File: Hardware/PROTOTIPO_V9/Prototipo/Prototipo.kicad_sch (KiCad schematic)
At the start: 1 part, among them U1 YAAJ_BluePill_Part_Like_SWD_B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

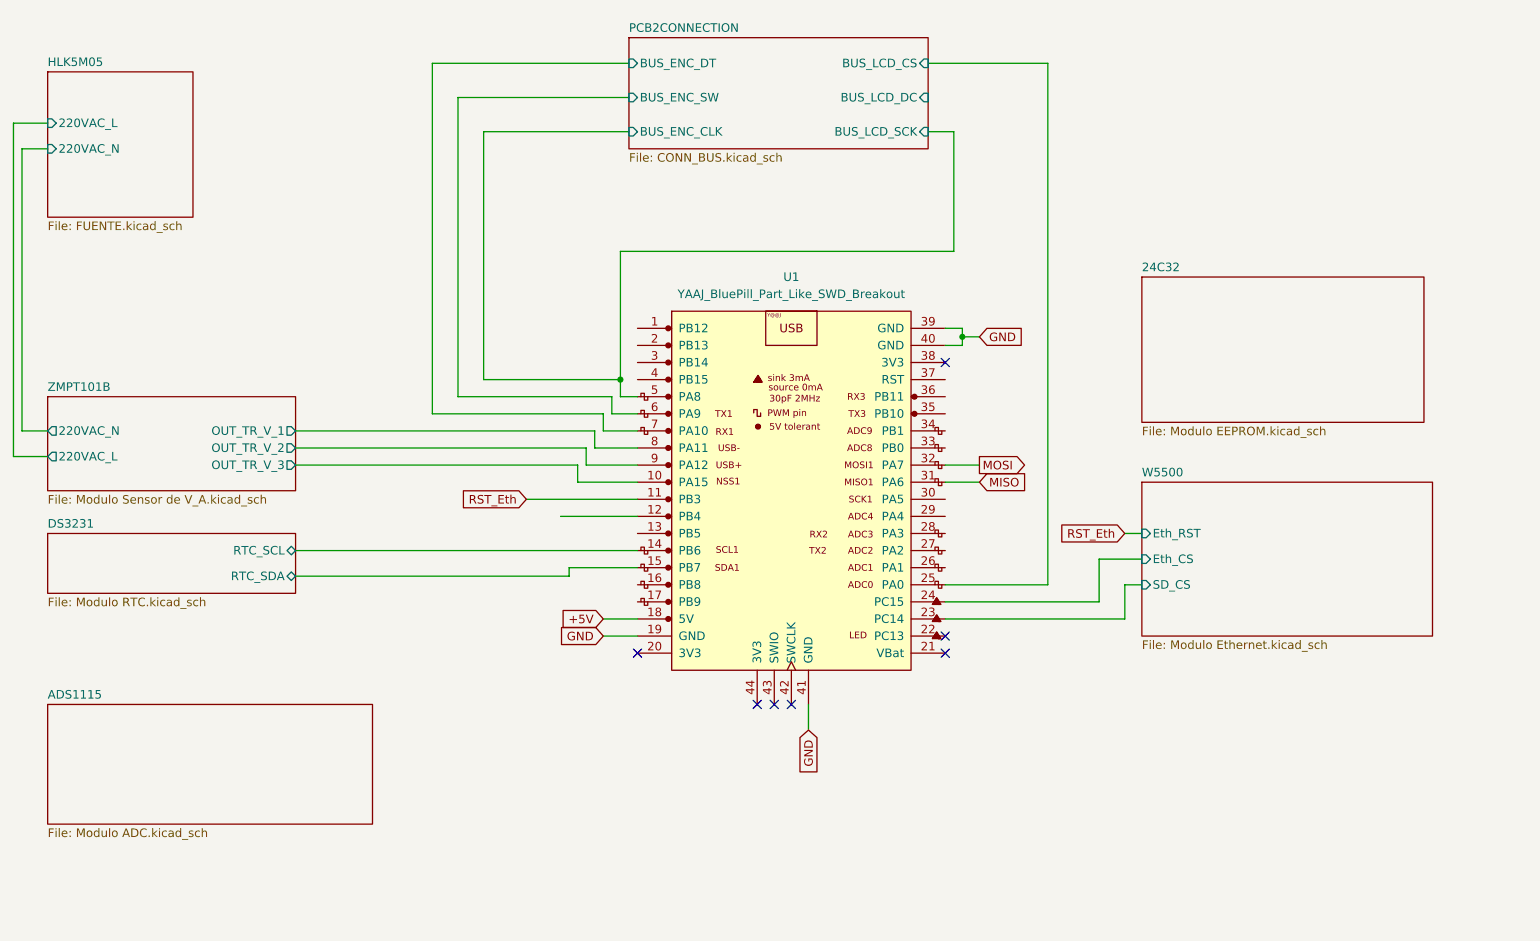
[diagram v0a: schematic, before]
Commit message: sch ILI9341 y sch ADS1115
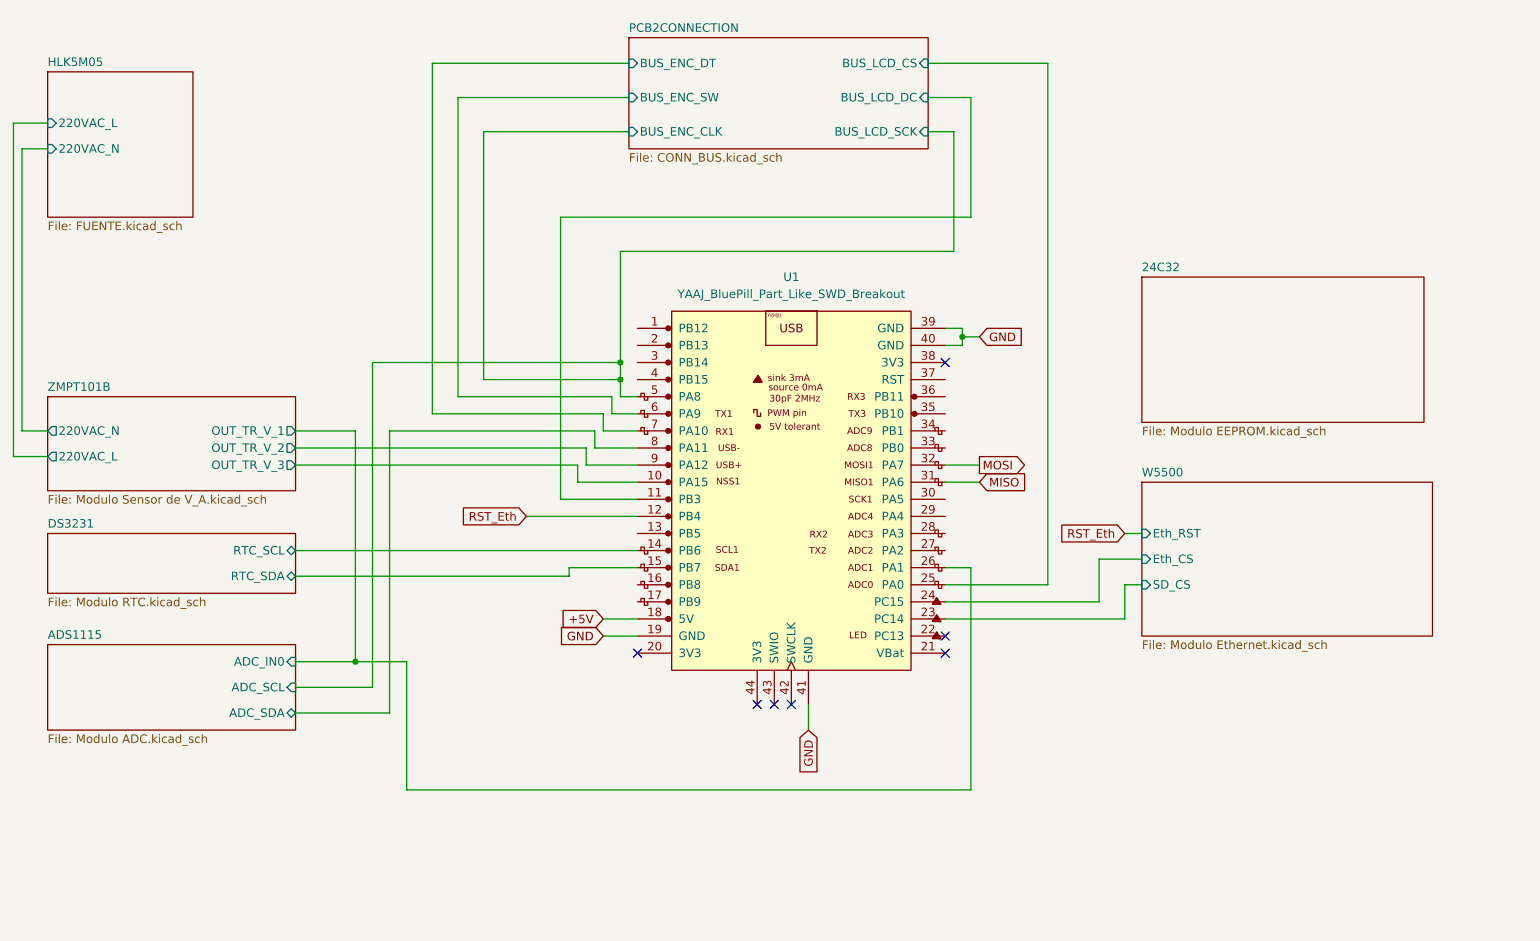
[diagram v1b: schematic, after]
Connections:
- net PCB2CONNECTION/BUS_LCD_DC: now also U1.11 (PB3)
- net RST_Eth: now also U1.12 (PB4); no longer U1.11 (PB3)
- net ADS1115/ADC_IN0: now reaches U1.26 (PA1)
- net PCB2CONNECTION/BUS_ENC_CLK renamed ADS1115/ADC_SCL
- net ZMPT101B/OUT_TR_V_1 renamed ADS1115/ADC_SDA
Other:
- sheet ADS1115 ports: added ADC_IN0, ADC_SCL, ADC_SDA; removed none
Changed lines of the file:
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@@
 	(paper "A4")
+	(junction
+		(at 82.55 125.73)
+		(diameter 0)
+		(color 0 0 0 0)
+	)
 	(junction
 		(at 172.72 77.47)
@@
 	)
 	(junction
+		(at 121.92 81.28)
+		(diameter 0)
+		(color 0 0 0 0)
+	)
+	(junction
 		(at 121.92 83.82)
 		(diameter 0)
@@
 	(wire
 		(pts
+			(xy 173.99 41.91) (xy 173.99 59.69)
+		)
+		(stroke
+			(width 0)
+			(type default)
+		)
+	)
+	(wire
+		(pts
 			(xy 36.83 91.44) (xy 33.02 91.44)
 		)
@@
 	(wire
 		(pts
+			(xy 85.09 81.28) (xy 85.09 129.54)
+		)
+		(stroke
+			(width 0)
+			(type default)
+		)
+	)
+	(wire
+		(pts
 			(xy 97.79 41.91) (xy 123.19 41.91)
 		)
@@
 	(wire
 		(pts
+			(xy 121.92 81.28) (xy 121.92 83.82)
+		)
+		(stroke
+			(width 0)
+			(type default)
+		)
+	)
+	(wire
+		(pts
+			(xy 85.09 129.54) (xy 73.66 129.54)
+		)
+		(stroke
+			(width 0)
+			(type default)
+		)
+	)
+	(wire
+		(pts
 			(xy 171.45 46.99) (xy 171.45 64.77)
 		)
@@
 	(wire
 		(pts
+			(xy 85.09 81.28) (xy 121.92 81.28)
+		)
+		(stroke
+			(width 0)
+			(type default)
+		)
+	)
+	(wire
+		(pts
 			(xy 73.66 113.03) (xy 114.3 113.03)
 		)
@@
 	(wire
 		(pts
+			(xy 87.63 91.44) (xy 87.63 133.35)
+		)
+		(stroke
+			(width 0)
+			(type default)
+		)
+	)
+	(wire
+		(pts
+			(xy 87.63 133.35) (xy 73.66 133.35)
+		)
+		(stroke
+			(width 0)
+			(type default)
+		)
+	)
+	(wire
+		(pts
 			(xy 114.3 111.76) (xy 124.46 111.76)
 		)
@@
 	(wire
 		(pts
+			(xy 113.03 59.69) (xy 113.03 101.6)
+		)
+		(stroke
+			(width 0)
+			(type default)
+		)
+	)
+	(wire
+		(pts
 			(xy 121.92 86.36) (xy 124.46 86.36)
 		)
@@
 	(wire
 		(pts
+			(xy 82.55 125.73) (xy 82.55 91.44)
+		)
+		(stroke
+			(width 0)
+			(type default)
+		)
+	)
+	(wire
+		(pts
+			(xy 113.03 101.6) (xy 124.46 101.6)
+		)
+		(stroke
+			(width 0)
+			(type default)
+		)
+	)
+	(wire
+		(pts
 			(xy 149.86 135.89) (xy 149.86 132.08)
 		)
@@
 	(wire
 		(pts
+			(xy 173.99 144.78) (xy 173.99 111.76)
+		)
+		(stroke
+			(width 0)
+			(type default)
+		)
+	)
+	(wire
+		(pts
 			(xy 172.72 77.47) (xy 175.26 77.47)
 		)
@@
 	(wire
 		(pts
+			(xy 90.17 125.73) (xy 90.17 144.78)
+		)
+		(stroke
+			(width 0)
+			(type default)
+		)
+	)
+	(wire
+		(pts
 			(xy 170.18 119.38) (xy 196.85 119.38)
 		)
@@
 	(wire
 		(pts
-			(xy 107.95 101.6) (xy 124.46 101.6)
+			(xy 107.95 104.14) (xy 124.46 104.14)
+		)
+		(stroke
+			(width 0)
+			(type default)
+		)
+	)
+	(wire
+		(pts
+			(xy 90.17 144.78) (xy 173.99 144.78)
 		)
 		(stroke
@@
 	(wire
 		(pts
+			(xy 173.99 59.69) (xy 113.03 59.69)
+		)
+		(stroke
+			(width 0)
+			(type default)
+		)
+	)
+	(wire
+		(pts
 			(xy 118.11 93.98) (xy 124.46 93.98)
 		)
@@
 	(wire
 		(pts
+			(xy 82.55 125.73) (xy 90.17 125.73)
+		)
+		(stroke
+			(width 0)
+			(type default)
+		)
+	)
+	(wire
+		(pts
+			(xy 173.99 111.76) (xy 170.18 111.76)
+		)
+		(stroke
+			(width 0)
+			(type default)
+		)
+	)
+	(wire
+		(pts
 			(xy 116.84 96.52) (xy 124.46 96.52)
 		)
@@
 	(wire
 		(pts
-			(xy 113.03 104.14) (xy 124.46 104.14)
-		)
-		(stroke
-			(width 0)
-			(type default)
-		)
-	)
-	(wire
-		(pts
 			(xy 33.02 49.53) (xy 36.83 49.53)
 		)
@@
 	(wire
 		(pts
-			(xy 73.66 91.44) (xy 118.11 91.44)
+			(xy 167.64 41.91) (xy 173.99 41.91)
+		)
+		(stroke
+			(width 0)
+			(type default)
+		)
+	)
+	(wire
+		(pts
+			(xy 73.66 91.44) (xy 82.55 91.44)
 		)
 		(stroke
@@
 	(wire
 		(pts
+			(xy 118.11 91.44) (xy 87.63 91.44)
+		)
+		(stroke
+			(width 0)
+			(type default)
+		)
+	)
+	(wire
+		(pts
 			(xy 172.72 77.47) (xy 172.72 78.74)
 		)
@@
 	(wire
 		(pts
-			(xy 121.92 64.77) (xy 121.92 83.82)
+			(xy 73.66 125.73) (xy 82.55 125.73)
+		)
+		(stroke
+			(width 0)
+			(type default)
+		)
+	)
+	(wire
+		(pts
+			(xy 121.92 64.77) (xy 121.92 81.28)
 		)
 		(stroke
@@
 	(global_label "RST_Eth"
 		(shape input)
-		(at 107.95 101.6 180)
+		(at 107.95 104.14 180)
 		(fields_autoplaced yes)
 		(effects
@@
 		)
 		(property "Intersheetrefs" "${INTERSHEET_REFS}"
-			(at 97.5264 101.6 0)
+			(at 97.5264 104.14 0)
 			(effects
 				(font
@@
 	)
 	(sheet
-		(at 36.83 132.08)
-		(size 48.26 17.78)
+		(at 36.83 123.19)
+		(size 36.83 12.7)
 		(exclude_from_sim no)
 		(in_bom yes)
@@
 		)
 		(property "Sheetname" "ADS1115"
-			(at 36.83 131.3684 0)
+			(at 36.83 122.4784 0)
 			(effects
 				(font
@@
 		)
 		(property "Sheetfile" "Modulo ADC.kicad_sch"
-			(at 36.83 150.4446 0)
+			(at 36.83 136.4746 0)
 			(effects
 				(font
@@
 			)
 		)
+		(pin "ADC_SCL" input
+			(at 73.66 129.54 0)
+			(effects
+				(font
+					(size 1.27 1.27)
+				)
+				(justify right)
+			)
+		)
+		(pin "ADC_SDA" bidirectional
+			(at 73.66 133.35 0)
+			(effects
+				(font
+					(size 1.27 1.27)
+				)
+				(justify right)
+			)
+		)
+		(pin "ADC_IN0" input
+			(at 73.66 125.73 0)
+			(effects
+				(font
+					(size 1.27 1.27)
+				)
+				(justify right)
+			)
+		)

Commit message: sch ILI9341
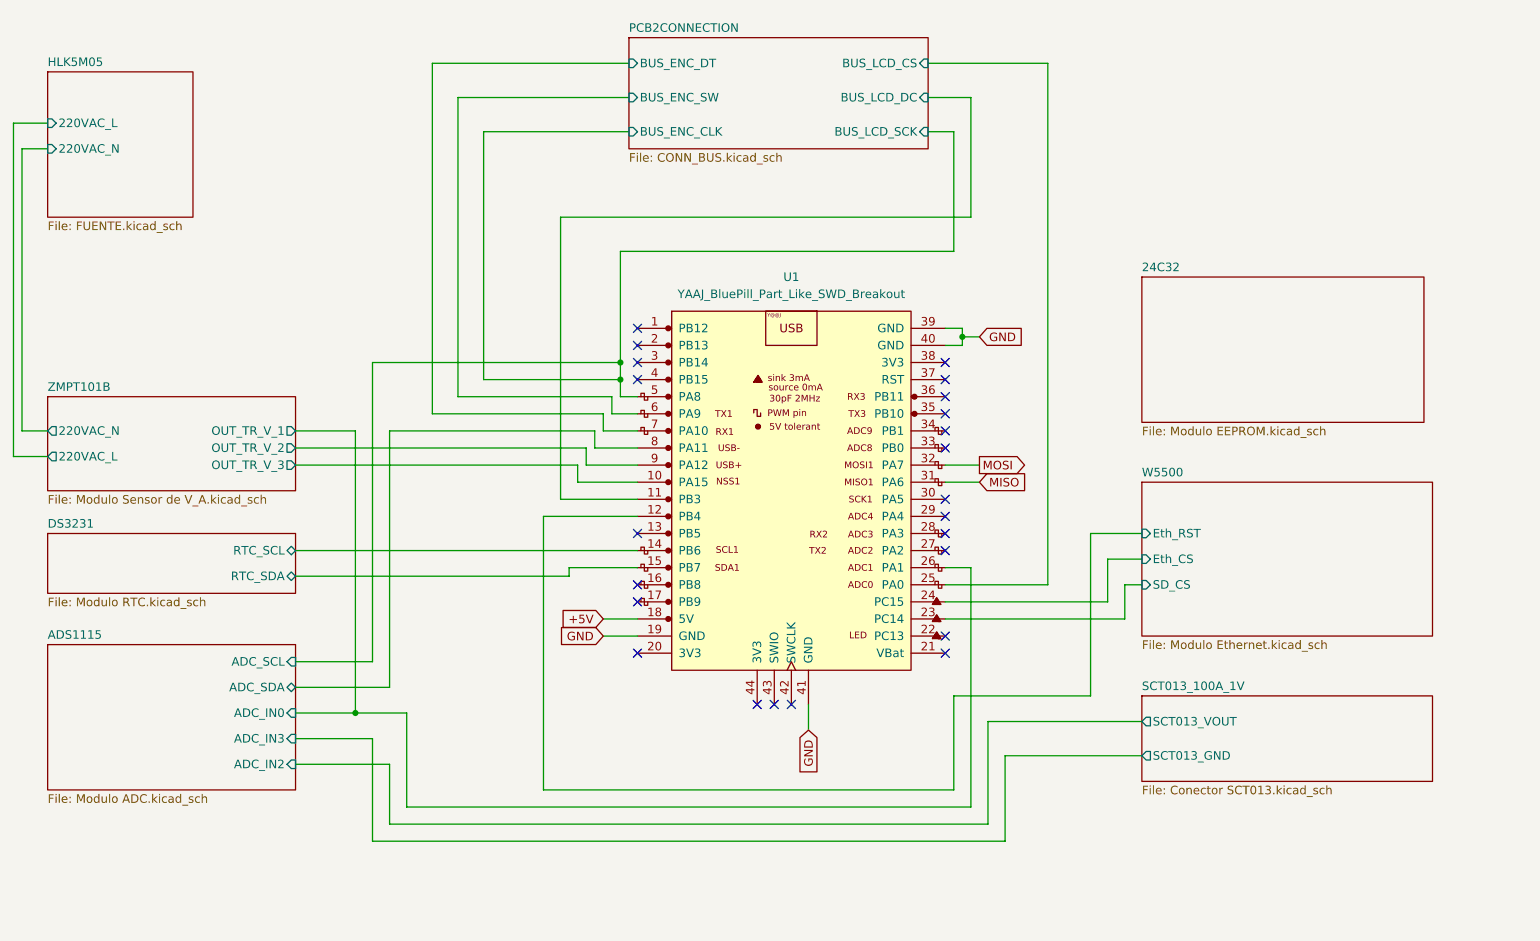
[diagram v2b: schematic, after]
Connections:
- net RST_Eth renamed W5500/Eth_RST
- no-connect marks 7 -> 23
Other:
- added sheet SCT013_100A_1V (Conector SCT013.kicad_sch)
- sheet ADS1115 ports: added ADC_IN2, ADC_IN3; removed none

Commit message: ERC: 0 errores
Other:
- sheet PCB2CONNECTION ports: added none; removed BUS_LCD_SCK
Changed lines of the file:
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@@
-	)
-	(junction
-		(at 121.92 81.28)
-		(diameter 0)
-		(color 0 0 0 0)
 	)
 	(junction
@@
 	(wire
 		(pts
-			(xy 171.45 46.99) (xy 171.45 64.77)
-		)
-		(stroke
-			(width 0)
-			(type default)
-		)
-	)
-	(wire
-		(pts
 			(xy 194.31 110.49) (xy 199.39 110.49)
 		)
@@
 	(wire
 		(pts
-			(xy 167.64 46.99) (xy 171.45 46.99)
-		)
-		(stroke
-			(width 0)
-			(type default)
-		)
-	)
-	(wire
-		(pts
 			(xy 115.57 96.52) (xy 115.57 99.06)
 		)
@@
 	(wire
 		(pts
-			(xy 171.45 64.77) (xy 121.92 64.77)
-		)
-		(stroke
-			(width 0)
-			(type default)
-		)
-	)
-	(wire
-		(pts
 			(xy 87.63 140.97) (xy 87.63 149.86)
 		)
@@
 		(pts
 			(xy 170.18 96.52) (xy 175.26 96.52)
-		)
-		(stroke
-			(width 0)
-			(type default)
-		)
-	)
-	(wire
-		(pts
-			(xy 121.92 64.77) (xy 121.92 81.28)
 		)
 		(stroke
@@
 			(effects
 				(font
-					(size 1.27 1.27)
-				)
-				(justify right)
-			)
-		)
-		(pin "BUS_LCD_SCK" input
-			(at 167.64 46.99 0)
-			(effects
-				(font

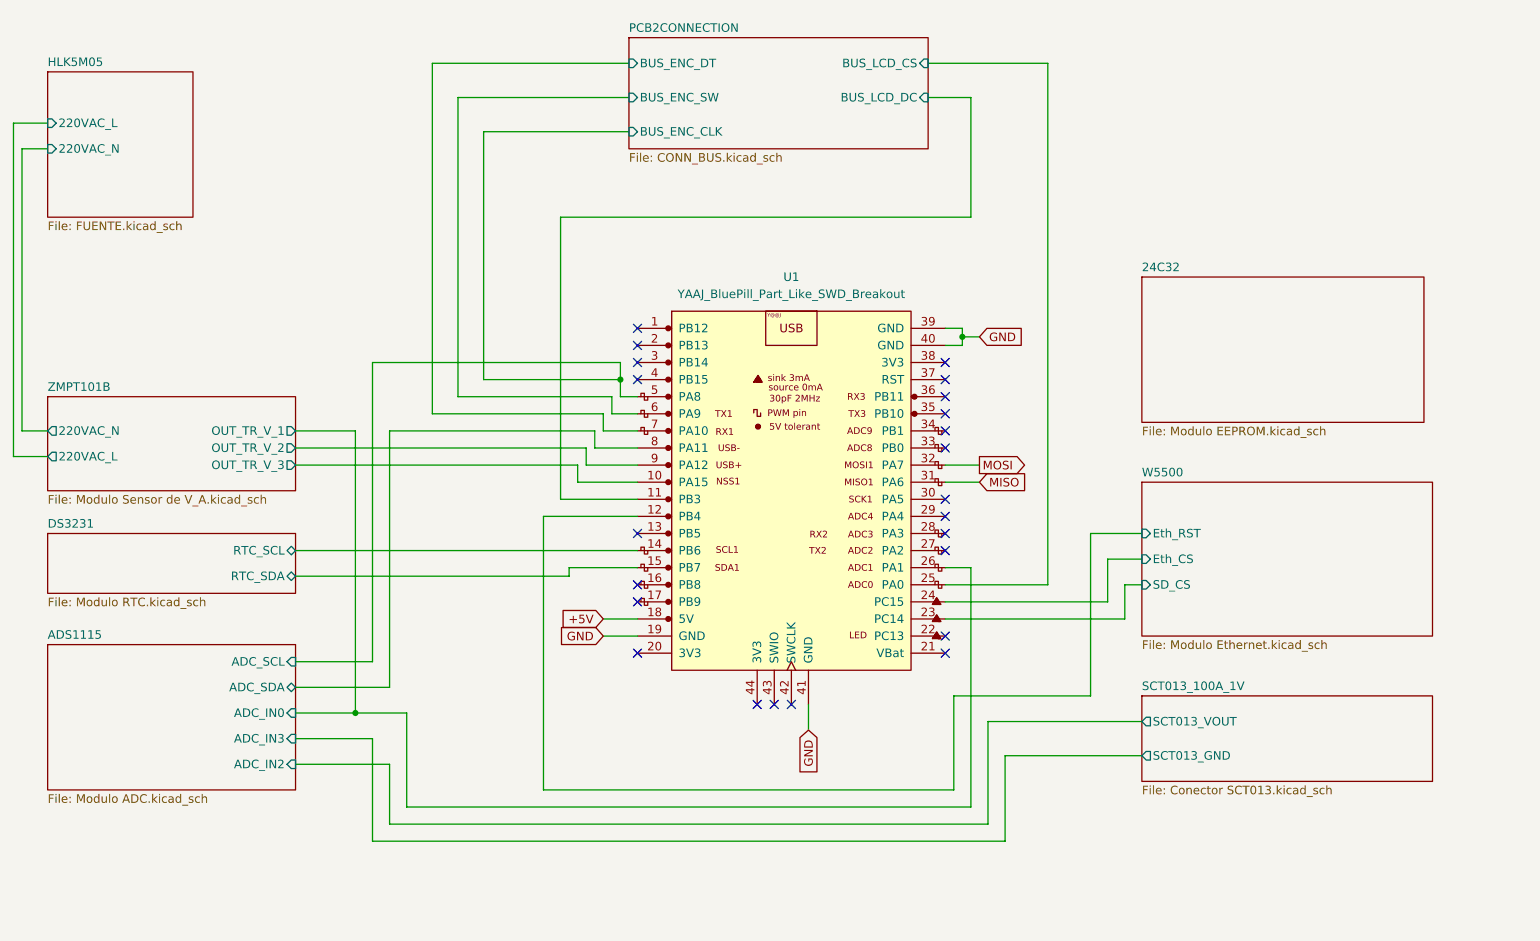
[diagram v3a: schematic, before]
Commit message: Esquematico TR de Corriente
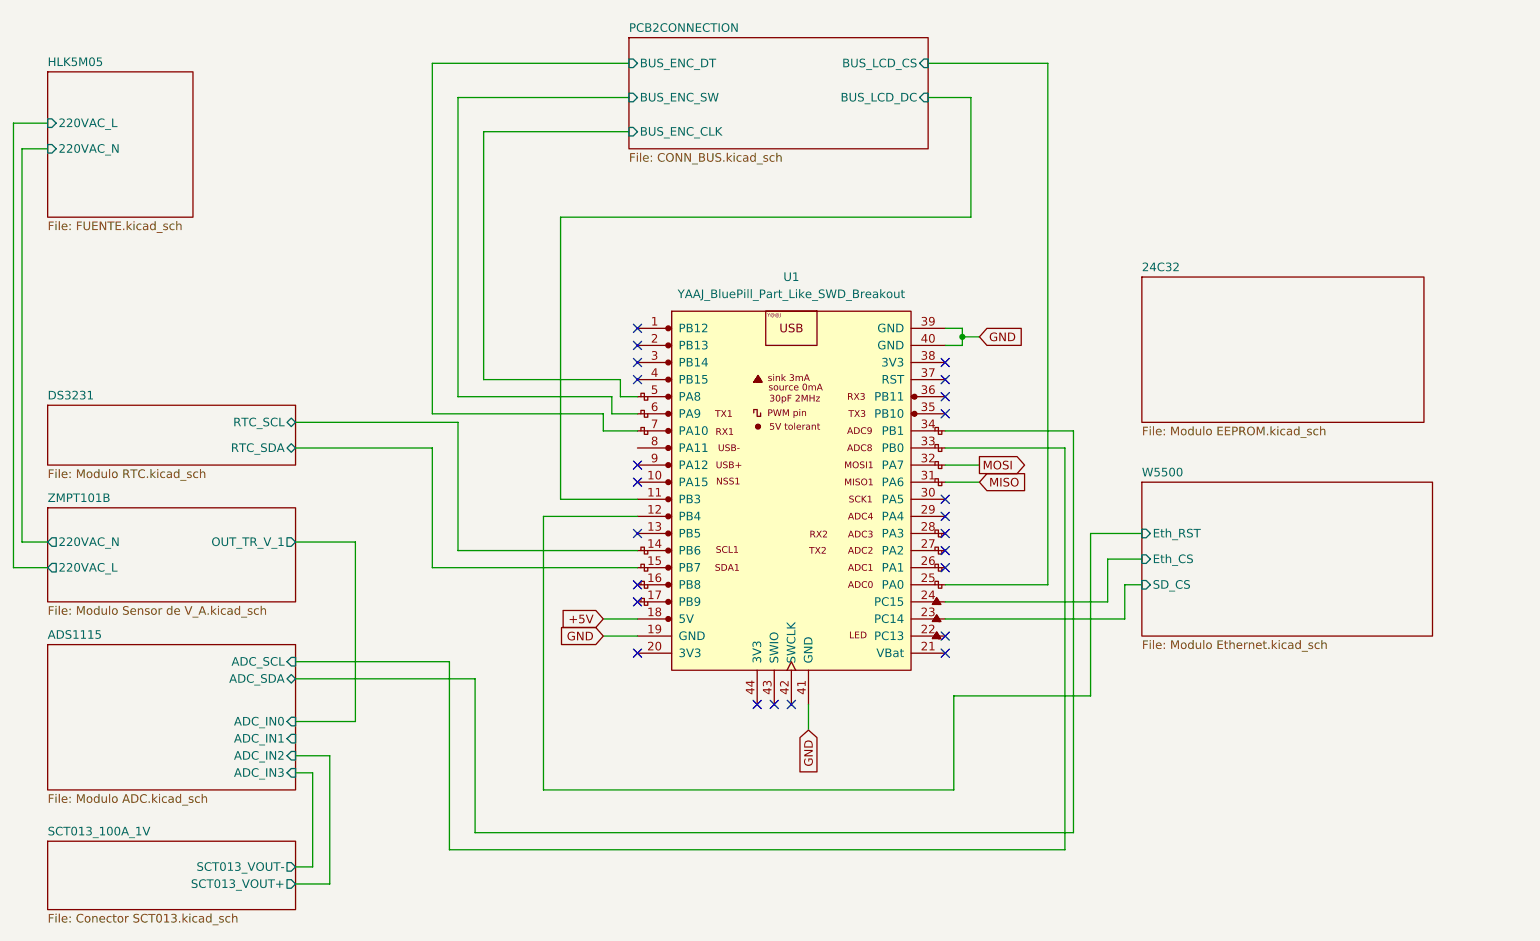
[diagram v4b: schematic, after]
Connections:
- net ADS1115/ADC_IN0: no longer U1.26 (PA1)
- net ADS1115/ADC_SCL: now also U1.33 (PB0); no longer U1.5 (PA8)
- net ADS1115/ADC_SDA: now also U1.34 (PB1); no longer U1.8 (PA11)
- net ZMPT101B/OUT_TR_V_2: no longer names the net of U1.9 (PA12)
- net ZMPT101B/OUT_TR_V_3: no longer names the net of U1.10 (PA15)
- new net PCB2CONNECTION/BUS_ENC_CLK: U1.5 (PA8)
- no-connect marks 23 -> 24
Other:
- sheet ADS1115 ports: added ADC_IN1; removed none
- sheet SCT013_100A_1V ports: added SCT013_VOUT+, SCT013_VOUT-; removed SCT013_GND, SCT013_VOUT
- sheet ZMPT101B ports: added none; removed OUT_TR_V_2, OUT_TR_V_3

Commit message: Esquematico completo v1.0
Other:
- removed sheet 24C32
- sheet ZMPT101B ports: added OUT_TR_V_1+, OUT_TR_V_1-; removed OUT_TR_V_1
